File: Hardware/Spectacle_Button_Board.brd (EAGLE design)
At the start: 44.5 x 73.7 mm, 53 parts, among them J17 AUDIO-JACK3, J19 FTDI_DEVICE, J20 AUDIO-JACK3, U1 CY8C4146LQI-S422, U2 3.3V/150mA

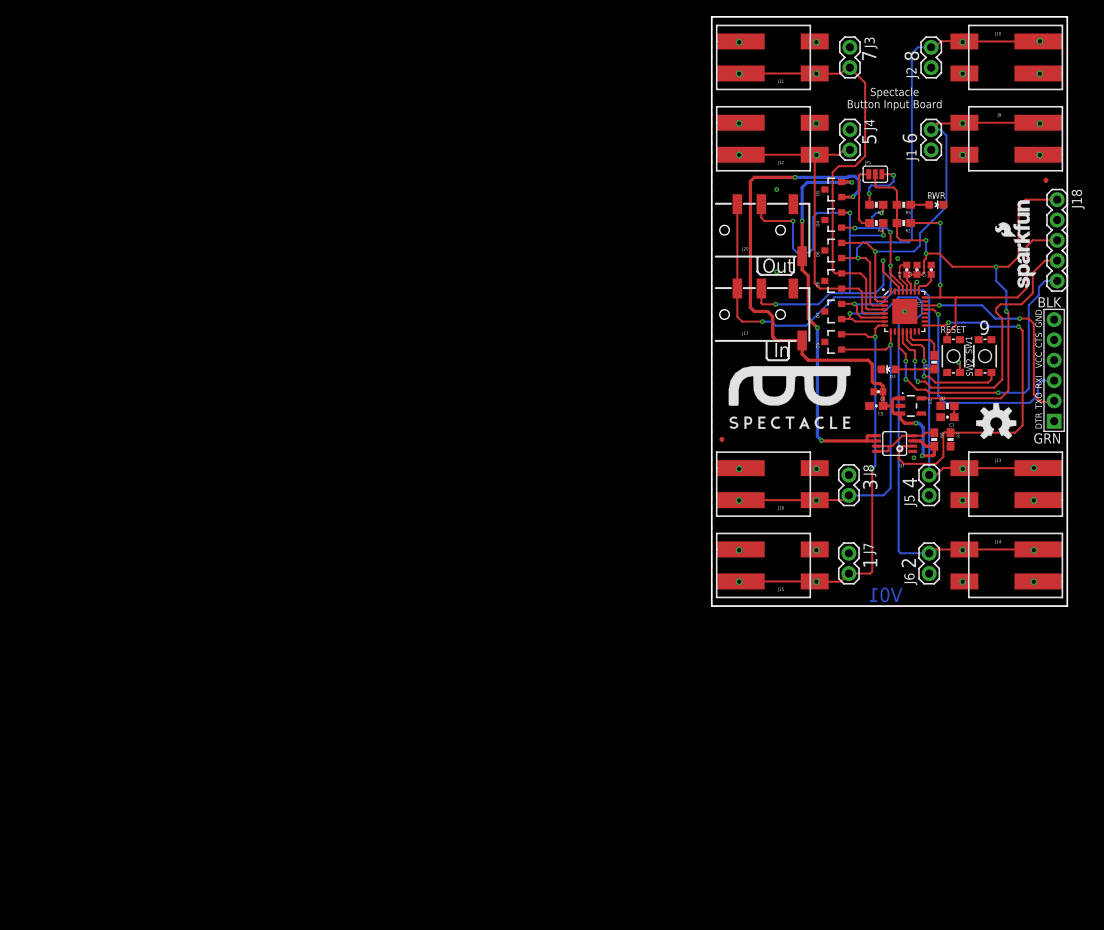
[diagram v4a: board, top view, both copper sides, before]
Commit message: Added I2C Mux hardware
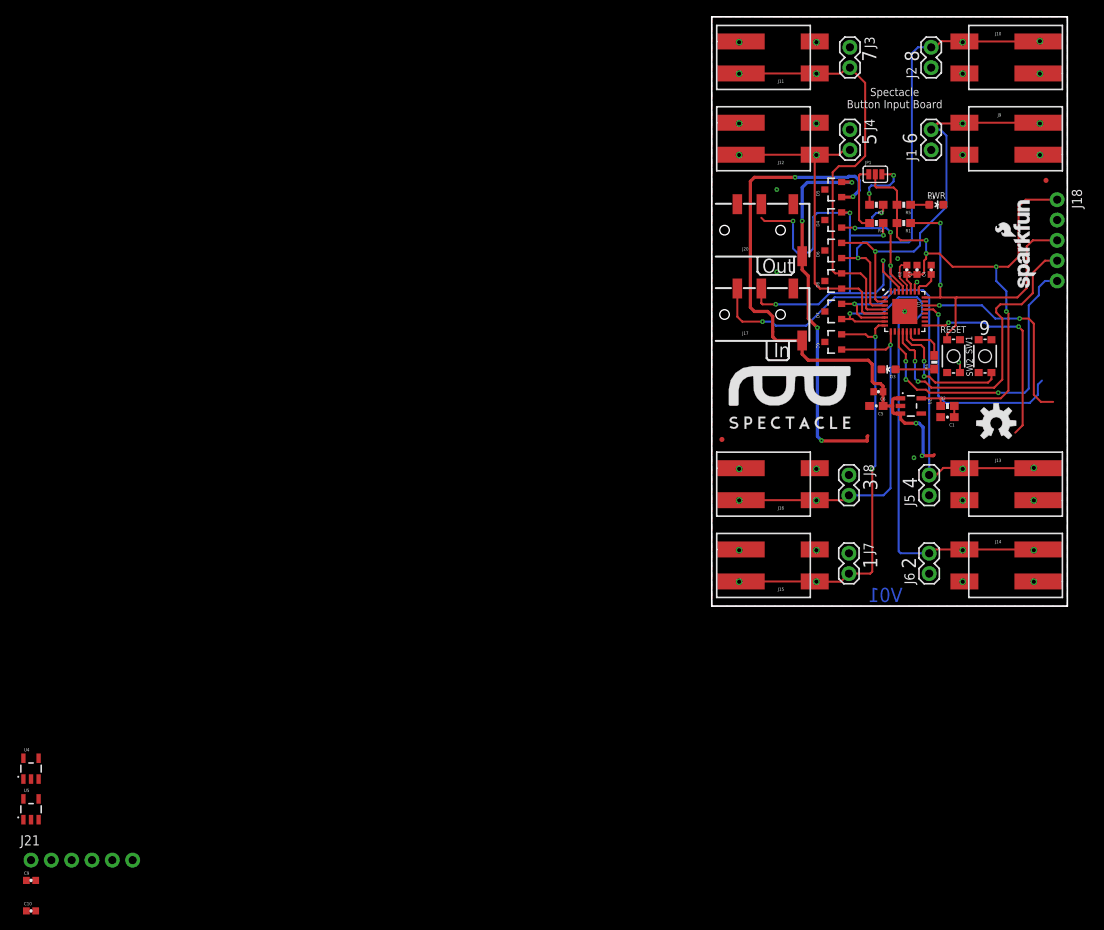
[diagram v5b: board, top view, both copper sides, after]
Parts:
- removed J19: FTDI_DEVICE, SparkFun-Connectors:FTDI_DEVICE_SIDE
- removed Q1: (no value), SparkFun-DiscreteSemi:MSOP8
- removed R7, R8: 10K, SparkFun-Resistors:0603-RES
- added C10, C9: 0.1uF, SparkFun-Capacitors:0402-CAP
- added J21: (no value), SparkFun-Connectors:1X06_NO_SILK
- added U4, U5: SN74LVC1G66, SparkFun-AnalogIC:SOT23-5
- J18: device SparkFun-Connectors:1X05 -> SparkFun-Connectors:1X05_NO_SILK
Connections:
- removed net N$26: Q1.4, Q1.7, Q1.8, R8.1
- removed net VOUT: D5.2, J20.EARTH, Q1.5, Q1.6
- removed net V_OUT_EN: Q1.2, R7.1, U1.17
- new net I2C_OUT_EN: U1.17, U4.4, U5.4
- new net SCL_OUT: J20.RING2, U4.2
- new net SDA_OUT: J20.RING1, U5.2
- net GND: now also C10.2, C9.2, J21.1, J21.2, U4.3, U5.3; no longer J19.P$5, J19.P$6, Q1.1, R7.2
- net RXI: now also J21.4; no longer J19.P$3
- net SCL: now also U4.1; no longer J20.RING2
- net SDA: now also U5.1; no longer J20.RING1
- net TXO: now also J21.5; no longer J19.P$2
- net VIN: now also C10.1, C9.1, D5.2, J20.EARTH, U4.5, U5.5; no longer Q1.3, R8.2
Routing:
- net VOUT: track 49.1 -> 0.00 mm, vias 4 -> 0
- net V_OUT_EN: track 47.1 -> 0.00 mm, vias 2 -> 0
- net VIN: track 78.5 -> 121.3 mm, vias 4 -> 8
- net I2C_OUT_EN: track 0.00 -> 25.9 mm, vias 0 -> 2
- net SCL: track 56.7 -> 46.2 mm
- net N$26: track 9.99 -> 0.00 mm
- net SDA: track 63.7 -> 62.0 mm
- net RXI: track 28.9 -> 27.3 mm

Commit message: Added I2C switching circuitry
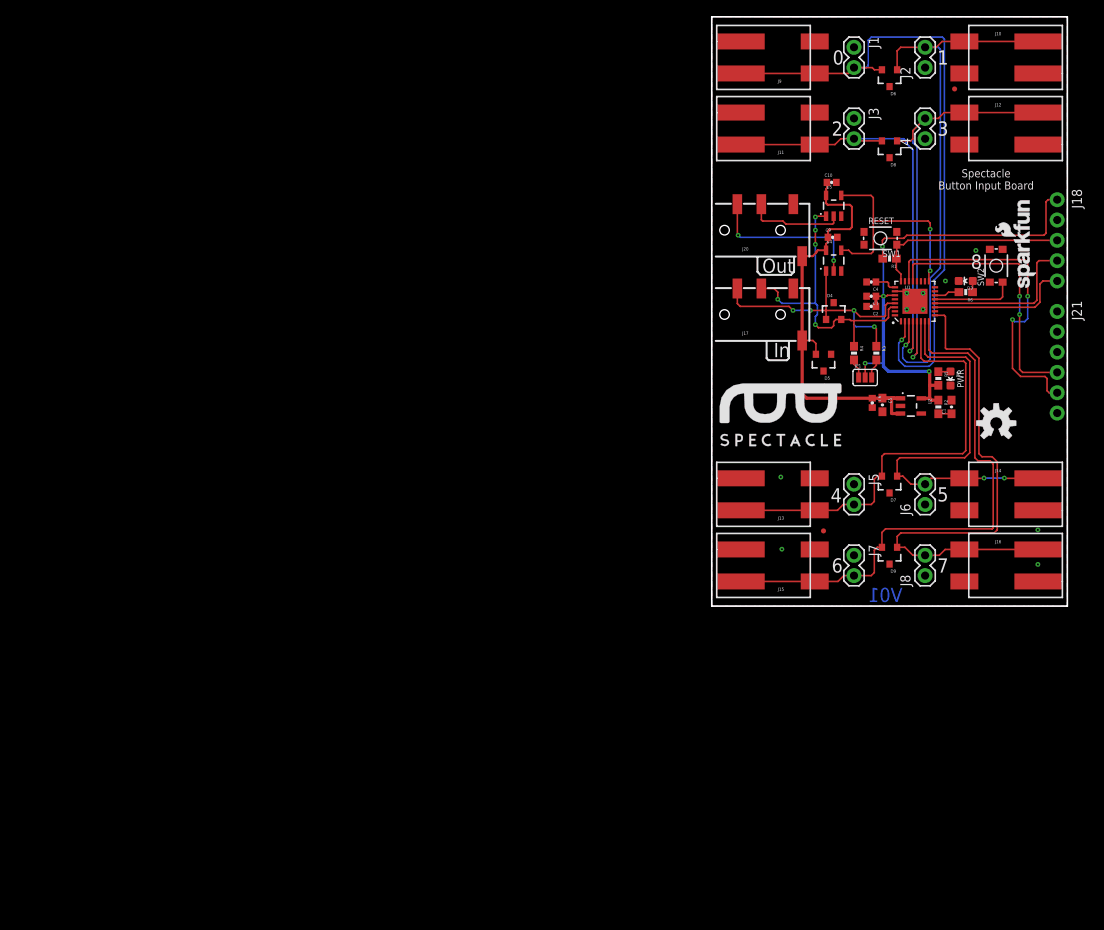
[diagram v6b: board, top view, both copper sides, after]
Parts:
- moved J21 145.5 mm to (43.2, 36.8), turned to 270 degrees
- moved C10 135.3 mm to (15.0, 53.0)
- moved C9 128.5 mm to (15.1, 46.1)
- moved U5 125.5 mm to (15.2, 50.0)
- moved U4 118.7 mm to (15.2, 43.2)
- moved J16 30.9 mm to (36.8, 5.08), turned to 180 degrees
- moved J9 30.9 mm to (7.62, 68.6), turned to 0 degrees
- moved J12 29.2 mm to (36.8, 59.7), turned to 180 degrees
- moved J13 29.2 mm to (7.62, 14.0), turned to 0 degrees
- moved D9 27.6 mm to (22.2, 6.35), turned to 180 degrees
- moved JP1 25.4 mm to (19.2, 28.6)
- moved D6 22.7 mm to (22.2, 66.0), turned to 180 degrees
- moved D7 22.7 mm to (22.2, 15.2), turned to 180 degrees
- moved R5 22.1 mm to (28.3, 28.4), turned to 270 degrees
- moved D2 21.8 mm to (29.8, 28.4), turned to 180 degrees
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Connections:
- net GND: now also SW1.2; no longer SW1.3
- net VIN: no longer D5.1
- net XRES: now also SW1.4; no longer SW1.1
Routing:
- net VIN: track 121.3 -> 55.2 mm, vias 8 -> 0
- net IN_0: track 52.0 -> 83.9 mm, vias 3 -> 1
- net SDA: track 62.0 -> 38.5 mm
- net SWD_DATA: track 38.5 -> 18.0 mm, vias 3 -> 0
- net SCL_OUT: track 0.00 -> 20.0 mm, vias 0 -> 2
- net SWD_CLK: track 39.4 -> 20.2 mm, vias 2 -> 0
- net IN_7: track 48.6 -> 67.1 mm, vias 3 -> 0
- net XRES: track 41.4 -> 25.1 mm, vias 2 -> 0
- net IN_5: track 67.4 -> 51.4 mm, vias 1 -> 2
- net IN_6: track 54.9 -> 69.7 mm, vias 4 -> 0
- net TXO: track 26.3 -> 40.6 mm
- net SDA_OUT: track 0.00 -> 12.1 mm
- net 3.3V: track 75.3 -> 64.0 mm
- net IN_3: track 45.0 -> 55.3 mm, vias 2 -> 1
- net SCL: track 46.2 -> 36.8 mm, vias 5 -> 4
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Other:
- board text added: "0"
- board text removed: "9"

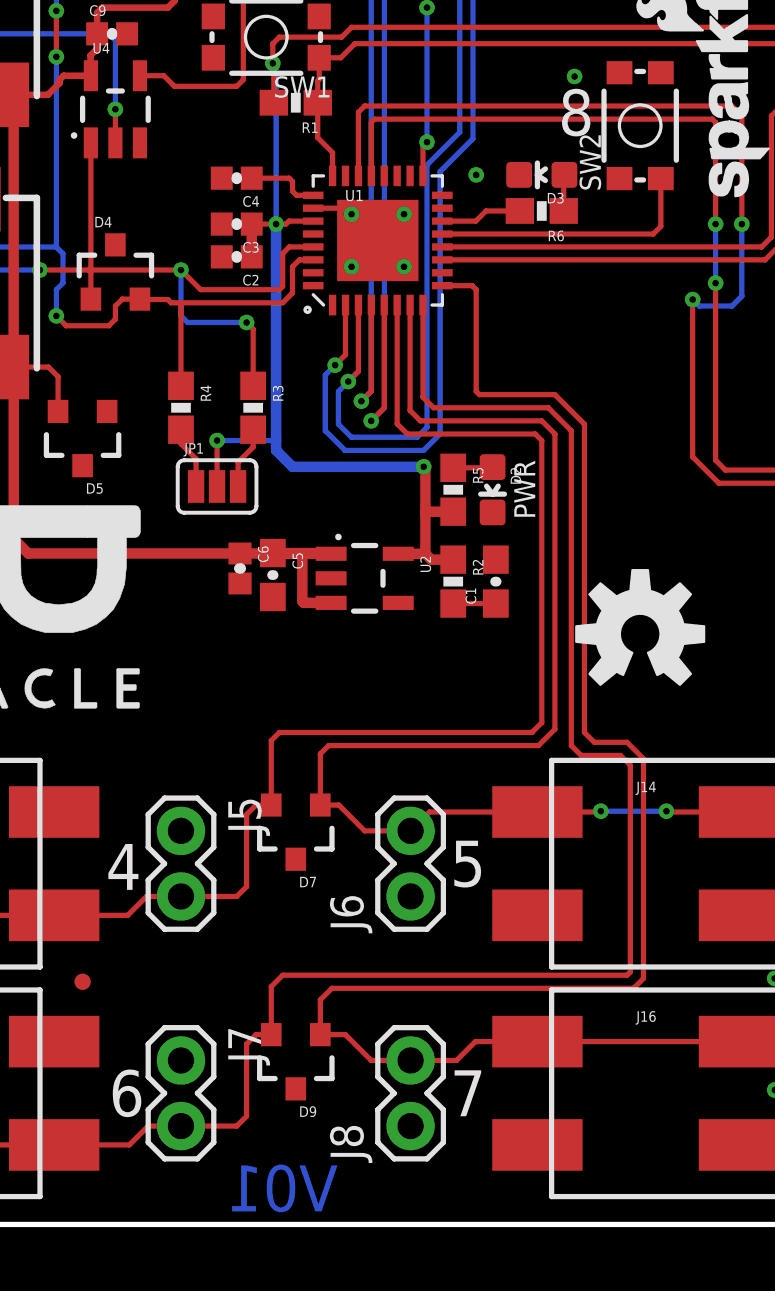
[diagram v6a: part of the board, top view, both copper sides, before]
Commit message: Fixes from review and checklist
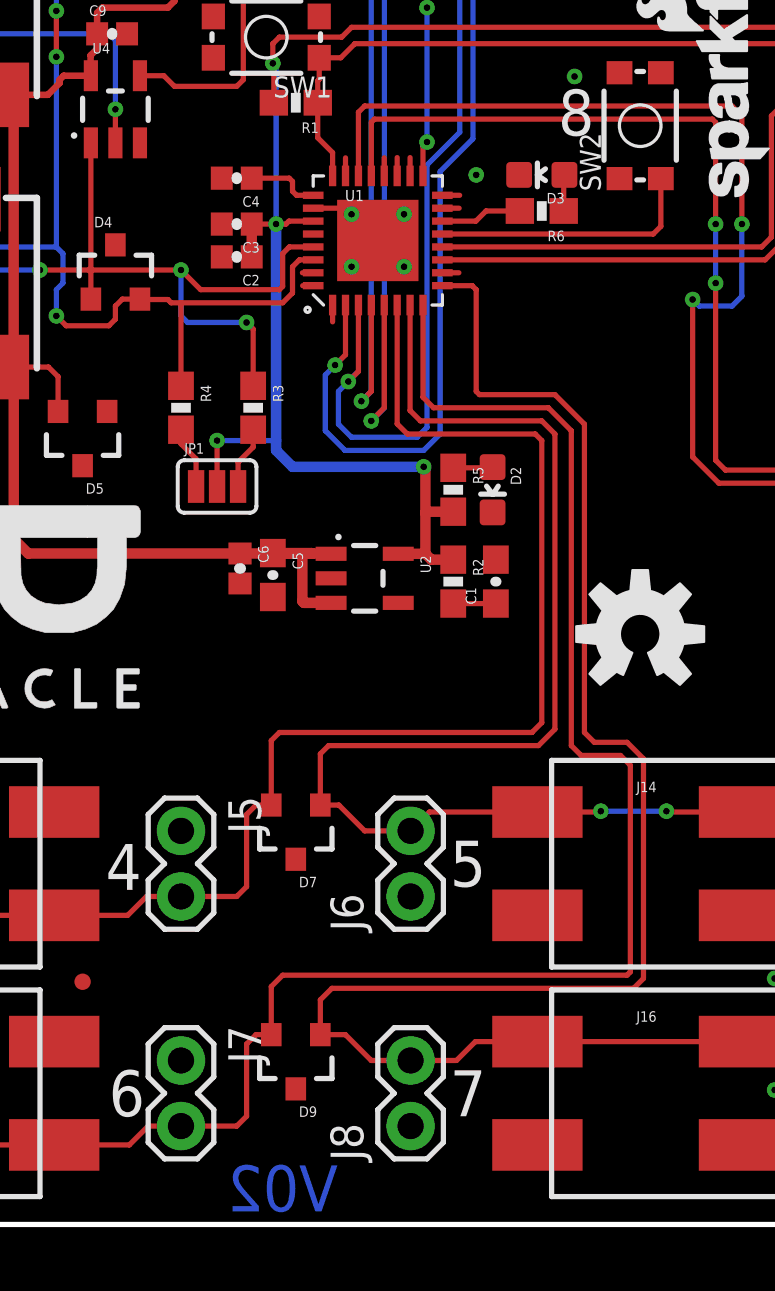
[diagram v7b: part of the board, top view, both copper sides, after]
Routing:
- net N$13: track 0.00 -> 0.70 mm
- net N$8: track 0.00 -> 0.69 mm
- net N$14: track 0.00 -> 0.69 mm
- net N$9: track 0.00 -> 0.66 mm
- net N$7: track 0.00 -> 0.62 mm
- net N$10: track 0.00 -> 0.56 mm
- net N$16: track 0.00 -> 0.55 mm
- net N$12: track 0.00 -> 0.55 mm
- net N$1: track 0.00 -> 0.52 mm
- net N$15: track 0.00 -> 0.50 mm
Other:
- board text added: "(typical)"
- board text added: "Dimensions in inches"
- board text added: "V02"
- board text removed: "PWR"
- board text removed: "V01"
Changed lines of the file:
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@@
 <?xml version="1.0" encoding="utf-8"?>
 <!DOCTYPE eagle SYSTEM "eagle.dtd">
-<eagle version="7.6.0">
+<eagle version="7.7.0">
 <drawing>
 <settings>
@@
 <grid distance="0.05" unitdist="inch" unit="inch" style="lines" multiple="1" display="yes" altdistance="0.005" altunitdist="inch" altunit="inch"/>
 <layers>
-<layer number="1" name="Top" color="4" fill="1" visible="no" active="yes"/>
-<layer number="2" name="Route2" color="1" fill="3" visible="no" active="yes"/>
-<layer number="15" name="Route15" color="4" fill="6" visible="no" active="yes"/>
+<layer number="1" name="Top" color="4" fill="1" visible="yes" active="yes"/>
+<layer number="2" name="Route2" color="1" fill="3" visible="yes" active="yes"/>
+<layer number="15" name="Route15" color="4" fill="6" visible="yes" active="yes"/>
 <layer number="16" name="Bottom" color="1" fill="1" visible="yes" active="yes"/>
 <layer number="17" name="Pads" color="2" fill="1" visible="yes" active="yes"/>
@@
 <layer number="19" name="Unrouted" color="6" fill="1" visible="yes" active="yes"/>
 <layer number="20" name="Dimension" color="15" fill="1" visible="yes" active="yes"/>
-<layer number="21" name="tPlace" color="16" fill="1" visible="no" active="yes"/>
+<layer number="21" name="tPlace" color="16" fill="1" visible="yes" active="yes"/>
 <layer number="22" name="bPlace" color="14" fill="1" visible="yes" active="yes"/>
-<layer number="23" name="tOrigins" color="15" fill="1" visible="no" active="yes"/>
+<layer number="23" name="tOrigins" color="15" fill="1" visible="yes" active="yes"/>
 <layer number="24" name="bOrigins" color="15" fill="1" visible="yes" active="yes"/>
-<layer number="25" name="tNames" color="7" fill="1" visible="no" active="yes"/>
-<layer number="26" name="bNames" color="7" fill="1" visible="no" active="yes"/>
-<layer number="27" name="tValues" color="7" fill="1" visible="no" active="yes"/>
-<layer number="28" name="bValues" color="7" fill="1" visible="no" active="yes"/>
-<layer number="29" name="tStop" color="7" fill="3" visible="no" active="yes"/>
-<layer number="30" name="bStop" color="7" fill="6" visible="no" active="yes"/>
-<layer number="31" name="tCream" color="7" fill="4" visible="no" active="yes"/>
-<layer number="32" name="bCream" color="7" fill="5" visible="no" active="yes"/>
-<layer number="39" name="tKeepout" color="4" fill="11" visible="no" active="yes"/>
-<layer number="40" name="bKeepout" color="1" fill="11" visible="no" active="yes"/>
-<layer number="41" name="tRestrict" color="4" fill="10" visible="no" active="yes"/>
-<layer number="42" name="bRestrict" color="1" fill="10" visible="no" active="yes"/>
-<layer number="43" name="vRestrict" color="2" fill="10" visible="no" active="yes"/>
-<layer number="44" name="Drills" color="7" fill="1" visible="no" active="yes"/>
-<layer number="45" name="Holes" color="7" fill="1" visible="no" active="yes"/>
-<layer number="46" name="Milling" color="3" fill="1" visible="no" active="yes"/>
-<layer number="47" name="Measures" color="7" fill="1" visible="no" active="yes"/>
-<layer number="48" name="Document" color="7" fill="1" visible="no" active="yes"/>
-<layer number="49" name="Reference" color="7" fill="1" visible="no" active="yes"/>
-<layer number="51" name="tDocu" color="6" fill="1" visible="no" active="yes"/>
-<layer number="52" name="bDocu" color="7" fill="1" visible="no" active="yes"/>
+<layer number="25" name="tNames" color="7" fill="1" visible="yes" active="yes"/>
+<layer number="26" name="bNames" color="7" fill="1" visible="yes" active="yes"/>
+<layer number="27" name="tValues" color="7" fill="1" visible="yes" active="yes"/>
+<layer number="28" name="bValues" color="7" fill="1" visible="yes" active="yes"/>
+<layer number="29" name="tStop" color="7" fill="3" visible="yes" active="yes"/>
+<layer number="30" name="bStop" color="7" fill="6" visible="yes" active="yes"/>
+<layer number="31" name="tCream" color="7" fill="4" visible="yes" active="yes"/>
+<layer number="32" name="bCream" color="7" fill="5" visible="yes" active="yes"/>
+<layer number="39" name="tKeepout" color="4" fill="11" visible="yes" active="yes"/>
+<layer number="40" name="bKeepout" color="1" fill="11" visible="yes" active="yes"/>
+<layer number="41" name="tRestrict" color="4" fill="10" visible="yes" active="yes"/>
+<layer number="42" name="bRestrict" color="1" fill="10" visible="yes" active="yes"/>
+<layer number="43" name="vRestrict" color="2" fill="10" visible="yes" active="yes"/>
+<layer number="44" name="Drills" color="7" fill="1" visible="yes" active="yes"/>
+<layer number="45" name="Holes" color="7" fill="1" visible="yes" active="yes"/>
+<layer number="46" name="Milling" color="3" fill="1" visible="yes" active="yes"/>
+<layer number="47" name="Measures" color="7" fill="1" visible="yes" active="yes"/>
+<layer number="48" name="Document" color="7" fill="1" visible="yes" active="yes"/>
+<layer number="49" name="Reference" color="7" fill="1" visible="yes" active="yes"/>
+<layer number="51" name="tDocu" color="6" fill="1" visible="yes" active="yes"/>
+<layer number="52" name="bDocu" color="7" fill="1" visible="yes" active="yes"/>
 <layer number="3" name="Route3" color="4" fill="3" visible="no" active="no"/>
 <layer number="4" name="Route4" color="1" fill="4" visible="no" active="no"/>
@@
 <vertex x="17.78" y="52.508"/>
 </polygon>
-<text x="19.558" y="2.286" size="1.778" layer="16" font="vector" ratio="15" rot="MR180">V01</text>
+<text x="19.558" y="2.286" size="1.778" layer="16" font="vector" ratio="15" rot="MR180">V02</text>
 <text x="-34.29" y="-16.51" size="1.778" layer="51" font="vector" ratio="15">Mike Hord and Dia Campbell</text>
-<text x="31.496" y="27.305" size="0.8128" layer="21" font="vector" ratio="15" rot="R90">PWR</text>
 <text x="19.558" y="47.752" size="0.8128" layer="21" font="vector" ratio="15">RESET</text>
 <text x="9.779" y="32.893" size="1.778" layer="21" font="vector" ratio="15" rot="R180">In</text>
@@
 <wire x1="9.906" y1="41.402" x2="6.096" y2="41.402" width="0.254" layer="21"/>
 <text x="15.113" y="67.691" size="1.778" layer="21" font="vector" ratio="15">0</text>
+<dimension x1="0" y1="0" x2="0" y2="5.08" x3="-5.08" y3="2.54" textsize="1.27" textratio="15" layer="47" dtype="vertical" unit="inch"/>
+<dimension x1="0" y1="0" x2="0" y2="13.97" x3="-8.89" y3="6.985" textsize="1.27" textratio="15" layer="47" dtype="vertical" unit="inch"/>
+<text x="-30.48" y="-7.62" size="1.27" layer="47" font="vector" ratio="15">Dimensions in inches</text>
+<text x="-12.7" y="2.54" size="1.27" layer="47" font="vector" ratio="15" rot="R90">(typical)</text>
 </plain>
 <attributes>
@@
 <attribute name="PROD_ID" value="IC-13549" x="7.62" y="60.198" size="1.778" layer="27" font="vector" ratio="15" display="off"/>
 </element>
-<element name="J21" library="SparkFun-Connectors" package="1X06_NO_SILK" value="" x="43.18" y="36.83" rot="R270">
-<attribute name="PROD_ID" value="CONN-08437" x="43.18" y="36.83" size="1.778" layer="27" font="vector" ratio="15" rot="R270" display="off"/>
-</element>
+<element name="J21" library="SparkFun-Connectors" package="1X06_NO_SILK" value="" x="43.18" y="36.83" rot="R270"/>
 <element name="C9" library="SparkFun-Capacitors" package="0402-CAP" value="0.1uF" x="15.113" y="46.101">
 <attribute name="PROD_ID" value="CAP-12416" x="15.113" y="46.101" size="1.778" layer="27" font="vector" ratio="15" display="off"/>
@@
 <wire x1="3.2" y1="46.457" x2="3.302" y2="46.355" width="0.2032" layer="1"/>
 </signal>
+<signal name="N$11">
+</signal>
+<signal name="N$1">
+<wire x1="24.15" y1="40.78" x2="24.15" y2="41.3" width="0.2032" layer="1"/>
+</signal>
+<signal name="N$7">
+<wire x1="25.65" y1="40.68" x2="25.65" y2="41.3" width="0.2032" layer="1"/>
+</signal>
+<signal name="N$8">
+<wire x1="26.15" y1="40.62" x2="26.15" y2="41.31" width="0.2032" layer="1"/>
+</signal>
+<signal name="N$9">
+<wire x1="26.65" y1="40.65" x2="26.65" y2="41.31" width="0.2032" layer="1"/>
+</signal>
+<signal name="N$10">
+<wire x1="28.01" y1="39.85" x2="28.57" y2="39.85" width="0.2032" layer="1"/>
+</signal>
+<signal name="N$12">
+<wire x1="28" y1="39.35" x2="28.55" y2="39.35" width="0.2032" layer="1"/>
+</signal>
+<signal name="N$13">
+<wire x1="27.84" y1="36.85" x2="28.54" y2="36.85" width="0.2032" layer="1"/>
+</signal>
+<signal name="N$14">
+<wire x1="23.65" y1="35.64" x2="23.65" y2="34.95" width="0.2032" layer="1"/>
+</signal>
+<signal name="N$15">
+<wire x1="22.99" y1="36.35" x2="22.49" y2="36.35" width="0.2032" layer="1"/>
+</signal>
+<signal name="N$16">
+<wire x1="23.03" y1="36.85" x2="22.48" y2="36.85" width="0.2032" layer="1"/>
+</signal>
 </signals>
